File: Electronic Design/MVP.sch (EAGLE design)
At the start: 35 parts, among them IC1 ACS712ELC-5A, IC2 ATMEGA328-PU, Q1 IRF9540, Q2 IRF9540, X1 16MHz

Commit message: made PCB a bit smaller
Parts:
- POT3: device resistor:R-TRIMM3299W -> resistor:R-TRIMM3296W
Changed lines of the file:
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@@
 <setting verticaltext="up"/>
 </settings>
-<grid distance="0.05" unitdist="inch" unit="inch" style="lines" multiple="1" display="no" altdistance="0.01" altunitdist="inch" altunit="inch"/>
+<grid distance="0.1" unitdist="inch" unit="inch" style="lines" multiple="1" display="no" altdistance="0.01" altunitdist="inch" altunit="inch"/>
 <layers>
 <layer number="1" name="Top" color="4" fill="1" visible="no" active="no"/>
@@
 <part name="Q1" library="transistor-power" deviceset="PMOSFET_P" device="TO220BV" value="IRF9540"/>
 <part name="Q2" library="transistor-power" deviceset="PMOSFET_P" device="TO220BV" value="IRF9540"/>
-<part name="POT3" library="resistor" deviceset="R-TRIMM" device="3299W" value="5k"/>
+<part name="POT3" library="resistor" deviceset="R-TRIMM" device="3296W" value="5k"/>
 <part name="R1" library="resistor" deviceset="R-EU_" device="VTA52" value="1k"/>
 <part name="SUPPLY22" library="supply2" deviceset="GND" device=""/>

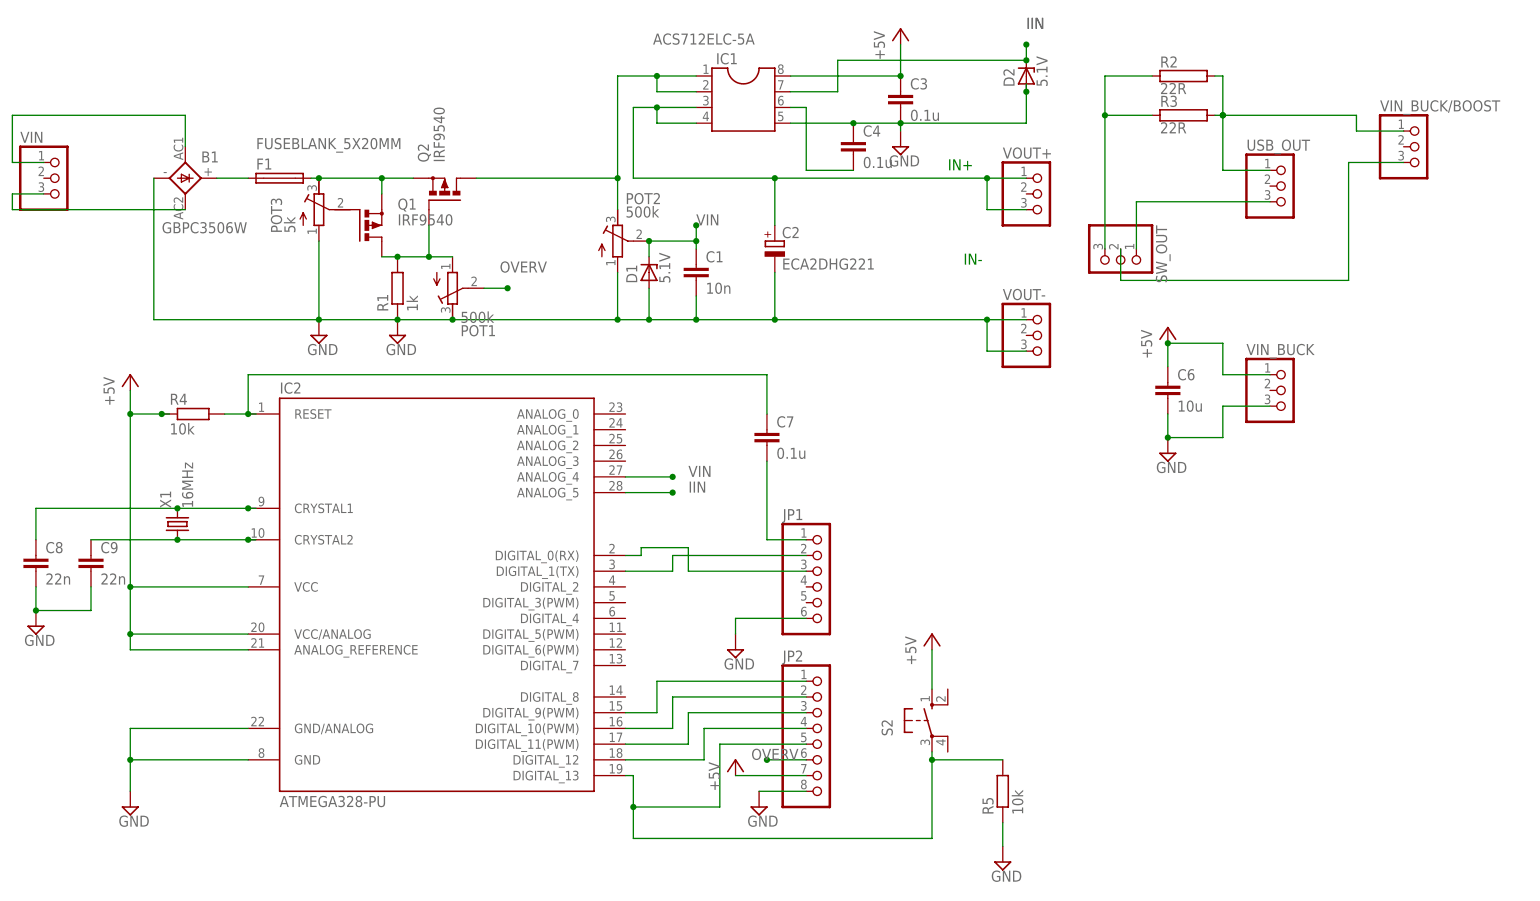
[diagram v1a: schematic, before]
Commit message: changed all pin headers from 7.62mm pitch to 5.08mm pitch
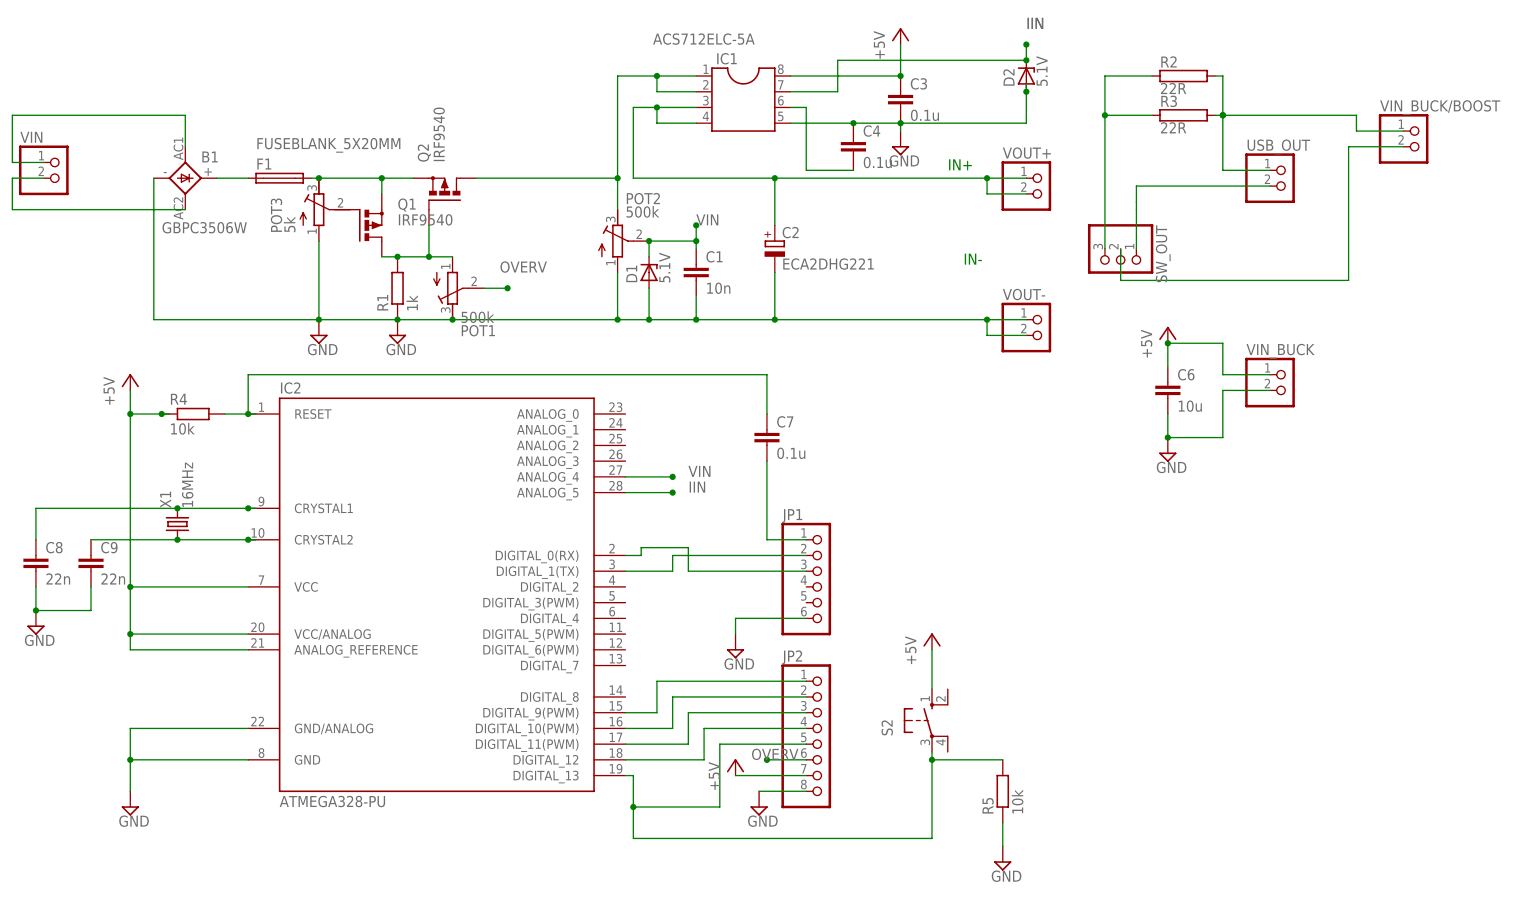
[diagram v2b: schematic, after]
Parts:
- USB_OUT, VIN, VIN_BUCK, VIN_BUCK/BOOST, VOUT+, VOUT-: device pinhead:PINHD-1X3 -> pinhead:PINHD-1X2
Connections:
- net GND: now also VIN_BUCK.2, VOUT-.2; no longer VIN_BUCK.3, VOUT-.3
- net M1S: now also VOUT+.2; no longer VOUT+.3
- net N$19: now also VIN.2; no longer VIN.3
- net N$22: now also VIN_BUCK/BOOST.2; no longer VIN_BUCK/BOOST.3
- net N$25: now also USB_OUT.2; no longer USB_OUT.3

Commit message: resolved clearnace issues and sorted a connection issue between pot3 and Q1
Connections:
- new net N$7: POT3.S, Q1.G
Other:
- moved on the sheet: F1, POT3
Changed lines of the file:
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@@
 <instance part="Q1" gate="G$1" x="-54.61" y="81.28"/>
 <instance part="Q2" gate="G$1" x="-41.91" y="86.36" rot="R90"/>
-<instance part="POT3" gate="G$1" x="-62.23" y="83.82"/>
+<instance part="POT3" gate="G$1" x="-66.04" y="83.82"/>
 <instance part="R1" gate="G$1" x="-49.53" y="71.12" rot="R90"/>
 <instance part="SUPPLY22" gate="GND" x="-49.53" y="63.5"/>
-<instance part="SUPPLY23" gate="GND" x="-62.23" y="63.5"/>
+<instance part="SUPPLY23" gate="GND" x="-66.04" y="63.5"/>
 <instance part="VIN" gate="G$1" x="-104.14" y="88.9"/>
 <instance part="VOUT+" gate="G$1" x="54.61" y="86.36"/>
-<instance part="F1" gate="G$1" x="-68.58" y="88.9" smashed="yes">
-<attribute name="NAME" x="-72.39" y="90.297" size="1.778" layer="95"/>
-<attribute name="VALUE" x="-72.39" y="93.599" size="1.778" layer="96"/>
+<instance part="F1" gate="G$1" x="-73.66" y="88.9" smashed="yes">
+<attribute name="NAME" x="-77.47" y="90.297" size="1.778" layer="95"/>
+<attribute name="VALUE" x="-77.47" y="93.599" size="1.778" layer="96"/>
 </instance>
 <instance part="SUPPLY29" gate="GND" x="-92.71" y="-12.7"/>
@@
 <pinref part="SUPPLY22" gate="GND" pin="GND"/>
 <junction x="-49.53" y="66.04"/>
-<wire x1="-62.23" y1="66.04" x2="-49.53" y2="66.04" width="0.1524" layer="91"/>
+<wire x1="-66.04" y1="66.04" x2="-49.53" y2="66.04" width="0.1524" layer="91"/>
 <pinref part="POT3" gate="G$1" pin="A"/>
-<wire x1="-62.23" y1="78.74" x2="-62.23" y2="66.04" width="0.1524" layer="91"/>
+<wire x1="-66.04" y1="78.74" x2="-66.04" y2="66.04" width="0.1524" layer="91"/>
 <pinref part="SUPPLY23" gate="GND" pin="GND"/>
-<junction x="-62.23" y="66.04"/>
+<junction x="-66.04" y="66.04"/>
 <pinref part="B1" gate="1" pin="-"/>
 <wire x1="-88.9" y1="88.9" x2="-88.9" y2="66.04" width="0.1524" layer="91"/>
-<wire x1="-62.23" y1="66.04" x2="-88.9" y2="66.04" width="0.1524" layer="91"/>
+<wire x1="-66.04" y1="66.04" x2="-88.9" y2="66.04" width="0.1524" layer="91"/>
 <pinref part="C2" gate="G$1" pin="-"/>
 <wire x1="11.43" y1="66.04" x2="11.43" y2="73.66" width="0.1524" layer="91"/>
@@
 <wire x1="-52.07" y1="88.9" x2="-46.99" y2="88.9" width="0.1524" layer="91"/>
 <pinref part="POT3" gate="G$1" pin="E"/>
-<wire x1="-62.23" y1="88.9" x2="-52.07" y2="88.9" width="0.1524" layer="91"/>
+<wire x1="-66.04" y1="88.9" x2="-52.07" y2="88.9" width="0.1524" layer="91"/>
 <junction x="-52.07" y="88.9"/>
-<wire x1="-62.23" y1="88.9" x2="-63.5" y2="88.9" width="0.1524" layer="91"/>
+<wire x1="-66.04" y1="88.9" x2="-68.58" y2="88.9" width="0.1524" layer="91"/>
 <pinref part="F1" gate="G$1" pin="2"/>
-<junction x="-62.23" y="88.9"/>
+<junction x="-66.04" y="88.9"/>
 </segment>
 </net>
@@
 <pinref part="B1" gate="1" pin="+"/>
 <pinref part="F1" gate="G$1" pin="1"/>
-<wire x1="-78.74" y1="88.9" x2="-73.66" y2="88.9" width="0.1524" layer="91"/>
 </segment>
 </net>
@@
 </segment>
 </net>
+<net name="N$7" class="0">
+<segment>
+<pinref part="Q1" gate="G$1" pin="G"/>
+<pinref part="POT3" gate="G$1" pin="S"/>
+<wire x1="-60.96" y1="83.82" x2="-59.69" y2="83.82" width="0.1524" layer="91"/>
+</segment>
+</net>

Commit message: corrected names and values of components
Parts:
- B1: value GBPC3506W -> KBPC610
- C2: value ECA2DHG221 -> 220uF
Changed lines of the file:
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@@
 <setting verticaltext="up"/>
 </settings>
-<grid distance="0.05" unitdist="inch" unit="inch" style="lines" multiple="1" display="no" altdistance="0.01" altunitdist="inch" altunit="inch"/>
+<grid distance="0.1" unitdist="inch" unit="inch" style="lines" multiple="1" display="no" altdistance="0.01" altunitdist="inch" altunit="inch"/>
 <layers>
-<layer number="1" name="Top" color="4" fill="1" visible="yes" active="no"/>
-<layer number="16" name="Bottom" color="1" fill="1" visible="yes" active="no"/>
-<layer number="17" name="Pads" color="2" fill="1" visible="yes" active="no"/>
-<layer number="18" name="Vias" color="2" fill="1" visible="yes" active="no"/>
-<layer number="19" name="Unrouted" color="6" fill="1" visible="yes" active="no"/>
-<layer number="20" name="Dimension" color="15" fill="1" visible="yes" active="no"/>
-<layer number="21" name="tPlace" color="7" fill="1" visible="yes" active="no"/>
-<layer number="22" name="bPlace" color="7" fill="1" visible="yes" active="no"/>
-<layer number="23" name="tOrigins" color="15" fill="1" visible="yes" active="no"/>
-<layer number="24" name="bOrigins" color="15" fill="1" visible="yes" active="no"/>
-<layer number="25" name="tNames" color="7" fill="1" visible="yes" active="no"/>
-<layer number="26" name="bNames" color="7" fill="1" visible="yes" active="no"/>
-<layer number="27" name="tValues" color="7" fill="1" visible="yes" active="no"/>
-<layer number="28" name="bValues" color="7" fill="1" visible="yes" active="no"/>
+<layer number="1" name="Top" color="4" fill="1" visible="no" active="no"/>
+<layer number="16" name="Bottom" color="1" fill="1" visible="no" active="no"/>
+<layer number="17" name="Pads" color="2" fill="1" visible="no" active="no"/>
+<layer number="18" name="Vias" color="2" fill="1" visible="no" active="no"/>
+<layer number="19" name="Unrouted" color="6" fill="1" visible="no" active="no"/>
+<layer number="20" name="Dimension" color="15" fill="1" visible="no" active="no"/>
+<layer number="21" name="tPlace" color="7" fill="1" visible="no" active="no"/>
+<layer number="22" name="bPlace" color="7" fill="1" visible="no" active="no"/>
+<layer number="23" name="tOrigins" color="15" fill="1" visible="no" active="no"/>
+<layer number="24" name="bOrigins" color="15" fill="1" visible="no" active="no"/>
+<layer number="25" name="tNames" color="7" fill="1" visible="no" active="no"/>
+<layer number="26" name="bNames" color="7" fill="1" visible="no" active="no"/>
+<layer number="27" name="tValues" color="7" fill="1" visible="no" active="no"/>
+<layer number="28" name="bValues" color="7" fill="1" visible="no" active="no"/>
 <layer number="29" name="tStop" color="7" fill="3" visible="no" active="no"/>
 <layer number="30" name="bStop" color="7" fill="6" visible="no" active="no"/>
@@
 <layer number="35" name="tGlue" color="7" fill="4" visible="no" active="no"/>
 <layer number="36" name="bGlue" color="7" fill="5" visible="no" active="no"/>
-<layer number="37" name="tTest" color="7" fill="1" visible="yes" active="no"/>
-<layer number="38" name="bTest" color="7" fill="1" visible="yes" active="no"/>
+<layer number="37" name="tTest" color="7" fill="1" visible="no" active="no"/>
+<layer number="38" name="bTest" color="7" fill="1" visible="no" active="no"/>
 <layer number="39" name="tKeepout" color="4" fill="11" visible="no" active="no"/>
 <layer number="40" name="bKeepout" color="1" fill="11" visible="no" active="no"/>
@@
 <layer number="44" name="Drills" color="7" fill="1" visible="no" active="no"/>
 <layer number="45" name="Holes" color="7" fill="1" visible="no" active="no"/>
-<layer number="46" name="Milling" color="3" fill="1" visible="yes" active="no"/>
-<layer number="47" name="Measures" color="7" fill="1" visible="yes" active="no"/>
-<layer number="48" name="Document" color="7" fill="1" visible="yes" active="no"/>
-<layer number="49" name="Reference" color="7" fill="1" visible="yes" active="no"/>
-<layer number="50" name="dxf" color="7" fill="1" visible="yes" active="no"/>
-<layer number="51" name="tDocu" color="7" fill="1" visible="yes" active="no"/>
-<layer number="52" name="bDocu" color="7" fill="1" visible="yes" active="no"/>
-<layer number="53" name="tGND_GNDA" color="7" fill="9" visible="yes" active="no"/>
-<layer number="54" name="bGND_GNDA" color="1" fill="9" visible="yes" active="no"/>
-<layer number="56" name="wert" color="7" fill="1" visible="yes" active="no"/>
+<layer number="46" name="Milling" color="3" fill="1" visible="no" active="no"/>
+<layer number="47" name="Measures" color="7" fill="1" visible="no" active="no"/>
+<layer number="48" name="Document" color="7" fill="1" visible="no" active="no"/>
+<layer number="49" name="Reference" color="7" fill="1" visible="no" active="no"/>
+<layer number="50" name="dxf" color="7" fill="1" visible="no" active="no"/>
+<layer number="51" name="tDocu" color="7" fill="1" visible="no" active="no"/>
+<layer number="52" name="bDocu" color="7" fill="1" visible="no" active="no"/>
+<layer number="53" name="tGND_GNDA" color="7" fill="9" visible="no" active="no"/>
+<layer number="54" name="bGND_GNDA" color="1" fill="9" visible="no" active="no"/>
+<layer number="56" name="wert" color="7" fill="1" visible="no" active="no"/>
 <layer number="90" name="Modules" color="5" fill="1" visible="yes" active="yes"/>
 <layer number="91" name="Nets" color="2" fill="1" visible="yes" active="yes"/>
@@
 </modules>
 <parts>
-<part name="B1" library="rectifier" deviceset="GBPC6" device="" value="GBPC3506W"/>
+<part name="B1" library="rectifier" deviceset="GBPC6" device="" value="KBPC610"/>
 <part name="C1" library="resistor" deviceset="C-EU" device="C1206K" value="10n"/>
-<part name="C2" library="resistor" deviceset="CPOL-EU" device="E3.5-10" value="ECA2DHG221"/>
+<part name="C2" library="resistor" deviceset="CPOL-EU" device="E3.5-10" value="220uF"/>
 <part name="IC1" library="mylibrary" deviceset="SOIC8" device="" value="ACS712ELC-5A"/>
 <part name="C3" library="resistor" deviceset="C-EU" device="C1206K" value="0.1u"/>

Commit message: connected VIN_BUCK/BOOST -ve to ground
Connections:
- removed net N$22: SW_OUT.2, VIN_BUCK/BOOST.2
- net GND: now also SW_OUT.2, VIN_BUCK/BOOST.2
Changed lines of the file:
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@@
 <setting verticaltext="up"/>
 </settings>
-<grid distance="0.1" unitdist="inch" unit="inch" style="lines" multiple="1" display="no" altdistance="0.01" altunitdist="inch" altunit="inch"/>
+<grid distance="0.05" unitdist="inch" unit="inch" style="lines" multiple="1" display="no" altdistance="0.01" altunitdist="inch" altunit="inch"/>
 <layers>
 <layer number="1" name="Top" color="4" fill="1" visible="no" active="no"/>
@@
 <part name="C4" library="resistor" deviceset="C-EU" device="C1206K" value="0.1u"/>
 <part name="SW_OUT" library="pinhead" deviceset="PINHD-1X3" device=""/>
+<part name="SUPPLY4" library="supply2" deviceset="GND" device=""/>
 </parts>
 <sheets>
@@
 <instance part="C4" gate="G$1" x="24.13" y="95.25"/>
 <instance part="SW_OUT" gate="A" x="67.31" y="74.93" rot="R270"/>
+<instance part="SUPPLY4" gate="GND" x="104.14" y="69.85"/>
 </instances>
 <busses>
@@
 <pinref part="SUPPLY6" gate="GND" pin="GND"/>
 </segment>
+<segment>
+<wire x1="67.31" y1="72.39" x2="104.14" y2="72.39" width="0.1524" layer="91"/>
+<wire x1="104.14" y1="72.39" x2="104.14" y2="93.98" width="0.1524" layer="91"/>
+<pinref part="SW_OUT" gate="A" pin="2"/>
+<wire x1="67.31" y1="72.39" x2="67.31" y2="77.47" width="0.1524" layer="91"/>
+<pinref part="VIN_BUCK/BOOST" gate="G$1" pin="2"/>
+<wire x1="113.03" y1="93.98" x2="104.14" y2="93.98" width="0.1524" layer="91"/>
+<pinref part="SUPPLY4" gate="GND" pin="GND"/>
+<junction x="104.14" y="72.39"/>
+</segment>
 </net>
 <net name="N$19" class="0">
@@
 </segment>
 </net>
-<net name="N$22" class="0">
-<segment>
-<wire x1="67.31" y1="72.39" x2="104.14" y2="72.39" width="0.1524" layer="91"/>
-<wire x1="104.14" y1="72.39" x2="104.14" y2="93.98" width="0.1524" layer="91"/>
-<pinref part="SW_OUT" gate="A" pin="2"/>
-<wire x1="67.31" y1="72.39" x2="67.31" y2="77.47" width="0.1524" layer="91"/>
-<pinref part="VIN_BUCK/BOOST" gate="G$1" pin="2"/>
-<wire x1="113.03" y1="93.98" x2="104.14" y2="93.98" width="0.1524" layer="91"/>
-</segment>
-</net>
